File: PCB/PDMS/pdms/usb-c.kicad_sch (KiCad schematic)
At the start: 10 parts, among them J6 2305018-2, U12 USBLC6-2SC6

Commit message: Clean-up of schematics
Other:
- note added: "USB-C Interface + SWD"
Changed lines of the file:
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@@
     (effects (font (size 2 2)) (justify left bottom))
+  )
+  (text "USB-C Interface + SWD" (at 99.949 129.032 0)
+    (effects (font (size 2 2) italic) (justify left bottom))
   )
   (global_label "SWCLK" (shape input) (at 48.895 59.69 0) (fields_autoplaced)

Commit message: WIP PCB folder structure and schematic clean-up
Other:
- company: (none) -> PGRacing Team
- title: (none) -> USB-C Interface + SWD
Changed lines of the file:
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@@
 (kicad_sch (version 20211123) (generator eeschema)
   (paper "A5")
+  (title_block
+    (title "USB-C Interface + SWD")
+    (rev "V4.2")
+    (company "PGRacing Team")
+    (comment 1 "Karol Pergoł")
+  )
   (junction (at 42.545 91.44) (diameter 0) (color 0 0 0 0)
   )

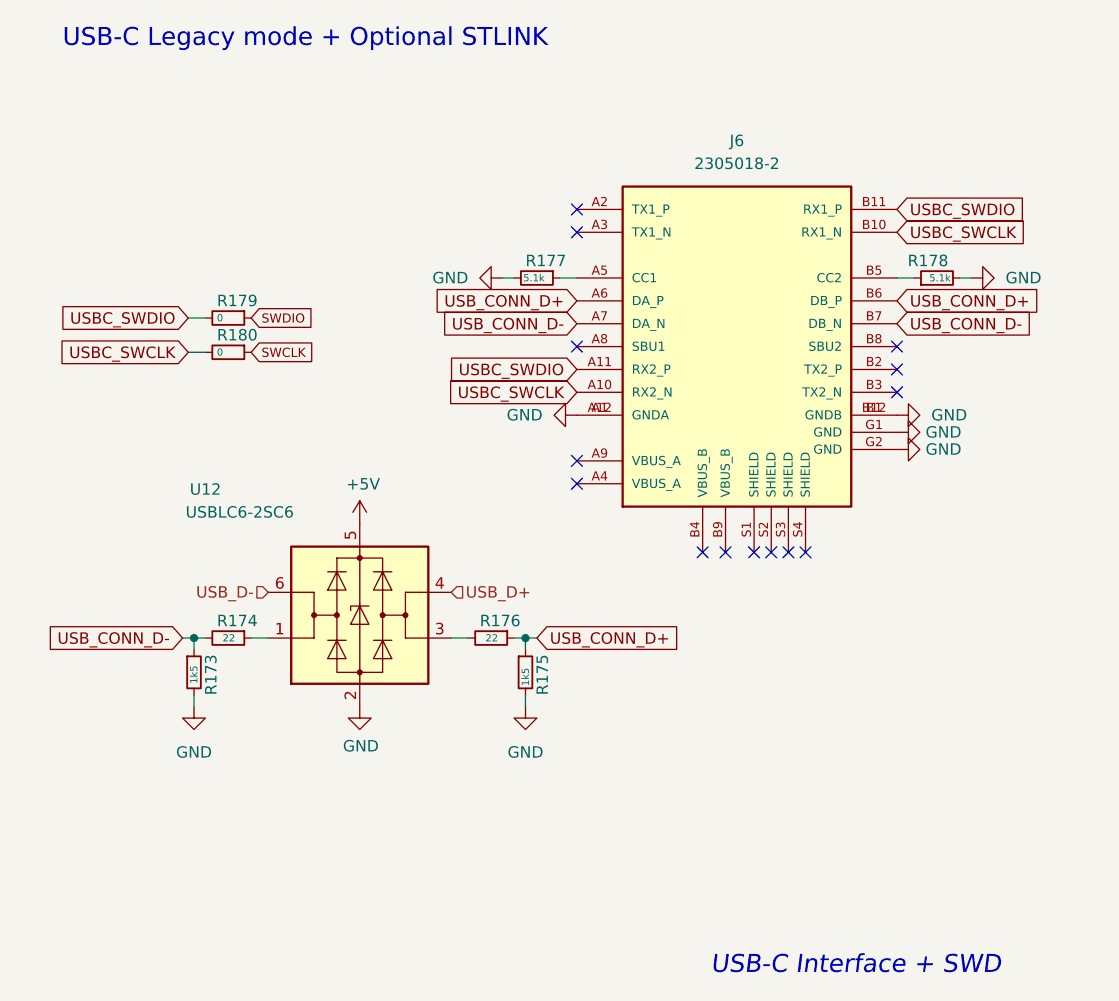
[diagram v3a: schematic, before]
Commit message: Added gerbers of PDMS v4.3, assembly docs, modified DNP parameters
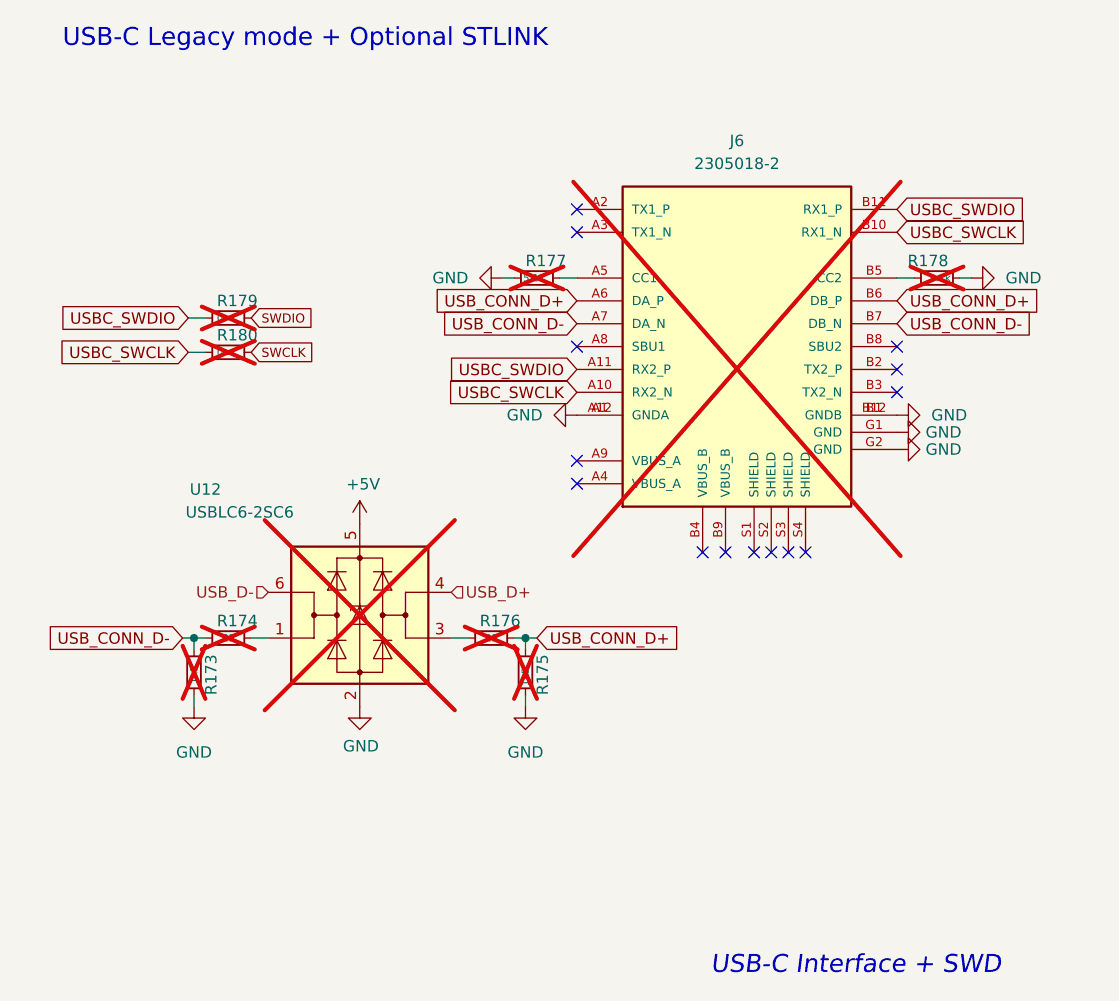
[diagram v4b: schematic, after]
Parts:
- J6, R173, R174, R175, R176, R177, R178, R179, R180, U12: now not fitted
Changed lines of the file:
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@@
 		(in_bom yes)
 		(on_board yes)
-		(dnp no)
+		(dnp yes)
 		(property "Reference" "R178"
 			(at 126.365 49.53 90)
@@
 		(in_bom yes)
 		(on_board yes)
-		(dnp no)
+		(dnp yes)
 		(fields_autoplaced yes)
 		(property "Reference" "J6"
@@
 		(in_bom yes)
 		(on_board yes)
-		(dnp no)
+		(dnp yes)
 		(property "Reference" "R180"
 			(at 45.085 57.785 90)
@@
 		(in_bom yes)
 		(on_board yes)
-		(dnp no)
+		(dnp yes)
 		(property "Reference" "R173"
 			(at 44.45 97.79 90)
@@
 		(in_bom yes)
 		(on_board yes)
-		(dnp no)
+		(dnp yes)
 		(property "Reference" "U12"
 			(at 43.815 74.93 0)
@@
 		(in_bom yes)
 		(on_board yes)
-		(dnp no)
+		(dnp yes)
 		(property "Reference" "R179"
 			(at 45.085 53.975 90)
@@
 		(in_bom yes)
 		(on_board yes)
-		(dnp no)
+		(dnp yes)
 		(property "Reference" "R176"
 			(at 74.295 89.535 90)
@@
 		(in_bom yes)
 		(on_board yes)
-		(dnp no)
+		(dnp yes)
 		(property "Reference" "R177"
 			(at 79.375 49.53 90)
@@
 		(in_bom yes)
 		(on_board yes)
-		(dnp no)
+		(dnp yes)
 		(property "Reference" "R174"
 			(at 45.085 89.535 90)
@@
 		(in_bom yes)
 		(on_board yes)
-		(dnp no)
+		(dnp yes)
 		(property "Reference" "R175"
 			(at 81.28 97.79 90)
